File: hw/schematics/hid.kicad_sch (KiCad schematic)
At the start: 124 parts, among them M1 SK8701-01-005-SENSOR, SW1 SW_Push, SW10 SW_Push, SW11 SW_Push, SW12 SW_Push, SW13 SW_Push, SW14 SW_Push, SW15 SW_Push, SW16 SW_Push, SW17 SW_Push, SW18 SW_Push, SW19 SW_Push, SW2 SW_Push, SW20 SW_Push, SW21 SW_Push, SW3 SW_Push, SW4 SW_Push, SW5 SW_Push, SW6 SW_Push, SW7 SW_Push, SW8 SW_Push, SW9 SW_Push, U3 ADS122S14

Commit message: Add a bunch of models and footprints
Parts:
- C10, C11, C9, rC10, rC11, rC9: footprint Alidade:0603 -> Alidade:C_0603_1608Metric
- R10, R11, R12, R13, R14, R15, R16, R7, R8, R9, rR10, rR11, rR12, rR13, rR14, rR15, rR16, rR7, rR8, rR9: footprint Alidade:0603 -> Alidade:R_0603_1608Metric
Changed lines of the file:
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@@
 			)
 		)
-		(property "Footprint" "Alidade:0603"
+		(property "Footprint" "Alidade:C_0603_1608Metric"
 			(at 158.75 219.71 0)
 			(effects
@@
 			)
 		)
-		(property "Footprint" "Alidade:0603"
+		(property "Footprint" "Alidade:R_0603_1608Metric"
 			(at 46.99 118.11 0)
 			(effects
@@
 			)
 		)
-		(property "Footprint" "Alidade:0603"
+		(property "Footprint" "Alidade:R_0603_1608Metric"
 			(at 342.9 199.39 0)
 			(effects
@@
 			)
 		)
-		(property "Footprint" "Alidade:0603"
+		(property "Footprint" "Alidade:C_0603_1608Metric"
 			(at 34.29 217.17 0)
 			(effects
@@
 			)
 		)
-		(property "Footprint" "Alidade:0603"
+		(property "Footprint" "Alidade:R_0603_1608Metric"
 			(at 304.8 200.66 0)
 			(effects
@@
 			)
 		)
-		(property "Footprint" "Alidade:0603"
+		(property "Footprint" "Alidade:C_0603_1608Metric"
 			(at 167.64 219.71 0)
 			(effects
@@
 			)
 		)
-		(property "Footprint" "Alidade:0603"
+		(property "Footprint" "Alidade:R_0603_1608Metric"
 			(at 374.65 118.11 0)
 			(effects
@@
 			)
 		)
-		(property "Footprint" "Alidade:0603"
+		(property "Footprint" "Alidade:C_0603_1608Metric"
 			(at 149.86 219.71 0)
 			(effects
@@
 			)
 		)
-		(property "Footprint" "Alidade:0603"
+		(property "Footprint" "Alidade:R_0603_1608Metric"
 			(at 279.4 200.66 0)
 			(effects
@@
 			)
 		)
-		(property "Footprint" "Alidade:0603"
+		(property "Footprint" "Alidade:R_0603_1608Metric"
 			(at 342.9 189.23 0)
 			(effects
@@
 			)
 		)
-		(property "Footprint" "Alidade:0603"
+		(property "Footprint" "Alidade:R_0603_1608Metric"
 			(at 46.99 102.87 0)
 			(effects
@@
 			)
 		)
-		(property "Footprint" "Alidade:0603"
+		(property "Footprint" "Alidade:R_0603_1608Metric"
 			(at 374.65 87.63 0)
 			(effects
@@
 			)
 		)
-		(property "Footprint" "Alidade:0603"
+		(property "Footprint" "Alidade:R_0603_1608Metric"
 			(at 279.4 190.5 0)
 			(effects
@@
 			)
 		)
-		(property "Footprint" "Alidade:0603"
+		(property "Footprint" "Alidade:R_0603_1608Metric"
 			(at 304.8 190.5 0)
 			(effects
@@
 			)
 		)
-		(property "Footprint" "Alidade:0603"
+		(property "Footprint" "Alidade:R_0603_1608Metric"
 			(at 76.2 246.38 0)
 			(effects
@@
 			)
 		)
-		(property "Footprint" "Alidade:0603"
+		(property "Footprint" "Alidade:R_0603_1608Metric"
 			(at 46.99 72.39 0)
 			(effects
@@
 			)
 		)
-		(property "Footprint" "Alidade:0603"
+		(property "Footprint" "Alidade:R_0603_1608Metric"
 			(at 368.3 189.23 0)
 			(effects
@@
 			)
 		)
-		(property "Footprint" "Alidade:0603"
+		(property "Footprint" "Alidade:R_0603_1608Metric"
 			(at 200.66 248.92 0)
 			(effects
@@
 			)
 		)
-		(property "Footprint" "Alidade:0603"
+		(property "Footprint" "Alidade:R_0603_1608Metric"
 			(at 368.3 199.39 0)
 			(effects
@@
 			)
 		)
-		(property "Footprint" "Alidade:0603"
+		(property "Footprint" "Alidade:R_0603_1608Metric"
 			(at 46.99 87.63 0)
 			(effects
@@
 			)
 		)
-		(property "Footprint" "Alidade:0603"
+		(property "Footprint" "Alidade:C_0603_1608Metric"
 			(at 25.4 217.17 0)
 			(effects
@@
 			)
 		)
-		(property "Footprint" "Alidade:0603"
+		(property "Footprint" "Alidade:R_0603_1608Metric"
 			(at 76.2 254 0)
 			(effects
@@
 			)
 		)
-		(property "Footprint" "Alidade:0603"
+		(property "Footprint" "Alidade:C_0603_1608Metric"
 			(at 43.18 217.17 0)
 			(effects
@@
 			)
 		)
-		(property "Footprint" "Alidade:0603"
+		(property "Footprint" "Alidade:R_0603_1608Metric"
 			(at 374.65 72.39 0)
 			(effects
@@
 			)
 		)
-		(property "Footprint" "Alidade:0603"
+		(property "Footprint" "Alidade:R_0603_1608Metric"
 			(at 200.66 256.54 0)
 			(effects
@@
 			)
 		)
-		(property "Footprint" "Alidade:0603"
+		(property "Footprint" "Alidade:R_0603_1608Metric"
 			(at 374.65 102.87 0)
 			(effects

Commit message: Various footprint updates
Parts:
- removed U3, rU3: ADS122S14, Alidade:RTE0016C-MFG, symbol Alidade:ADS122S14
- added U3, rU3: ADS122S14IRTER, Alidade:WQFN16_3X3, symbol Alidade:ADS122S14IRTER
- SWD1, rSWD1: footprint (none) -> Alidade:228ADS2
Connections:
- net ADCCS: now also U3.9 (CS)
- net AIN0: now also U3.1 (AIN0)
- net AIN1: now also U3.2 (AIN1)
- net AVDD: now also U3.15 (AVDD)
- net DRDY: now also U3.8 (AIN7/GPIO3/DRDY/CLK)
- net DVDD: now also U3.13 (DVDD)
- net FAULT: now also U3.7 (AIN6/GPIO2/FAULT)
- net GND: now also U3.14 (GND), U3.TP
- net MISO: now also U3.10 (SDO/DRDY)
- net MOSI: now also U3.11 (SDI)
- net REFN: now also U3.6 (AIN5/REFN/GPIO1)
- net REFP: now also U3.5 (AIN4/REFP/GPIO0)
- net SCK: now also U3.12 (SCK)
- net rADCCS: now also rU3.9 (CS)
- net rAIN0: now also rU3.1 (AIN0)
- net rAIN1: now also rU3.2 (AIN1)
- net rAVDD: now also rU3.15 (AVDD)
- net rDRDY: now also rU3.8 (AIN7/GPIO3/DRDY/CLK)
- net rDVDD: now also rU3.13 (DVDD)
- net rFAULT: now also rU3.7 (AIN6/GPIO2/FAULT)
- net rGND: now also rU3.14 (GND), rU3.TP
- net rMISO: now also rU3.10 (SDO/DRDY)
- net rMOSI: now also rU3.11 (SDI)
- net rREFN: now also rU3.6 (AIN5/REFN/GPIO1)
- net rREFP: now also rU3.5 (AIN4/REFP/GPIO0)
- net rSCK: now also rU3.12 (SCK)
- net at R15.2, R16.1: now also U3.3 (AIN2)
- net at rC11.1: now also rU3.16 (REFOUT)
- net at C11.1: now also U3.16 (REFOUT)
- net at rR15.2, rR16.1: now also rU3.3 (AIN2)

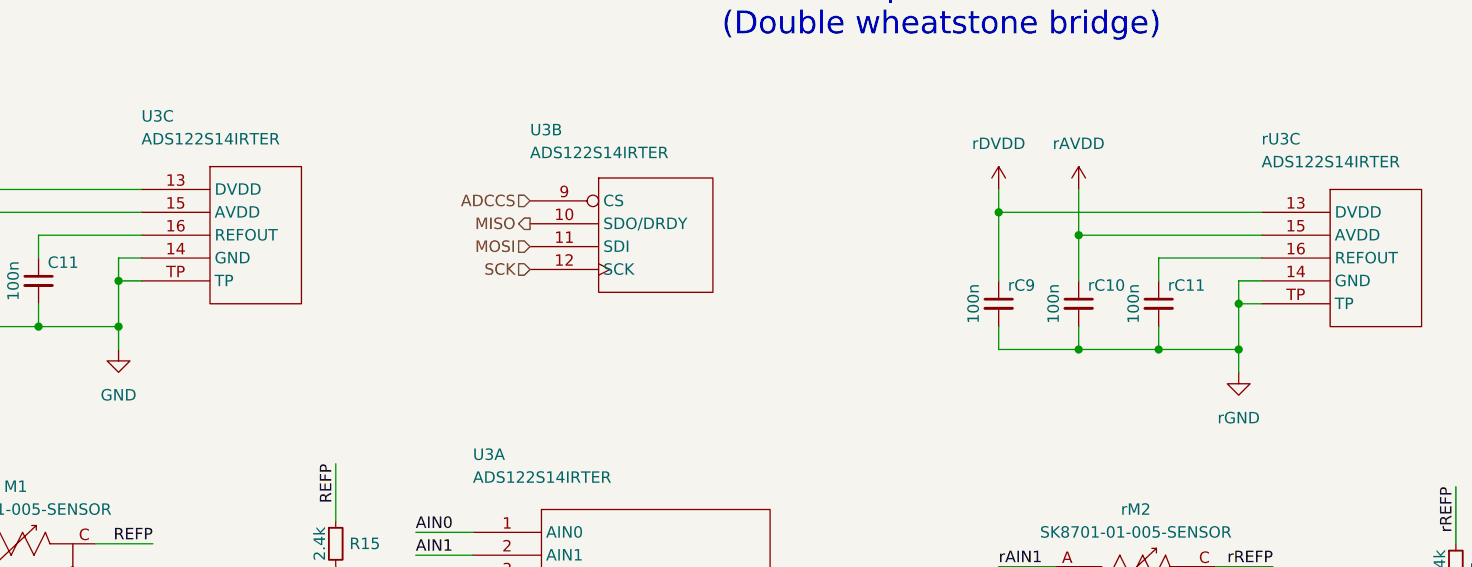
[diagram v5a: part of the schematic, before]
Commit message: Fix missing pads
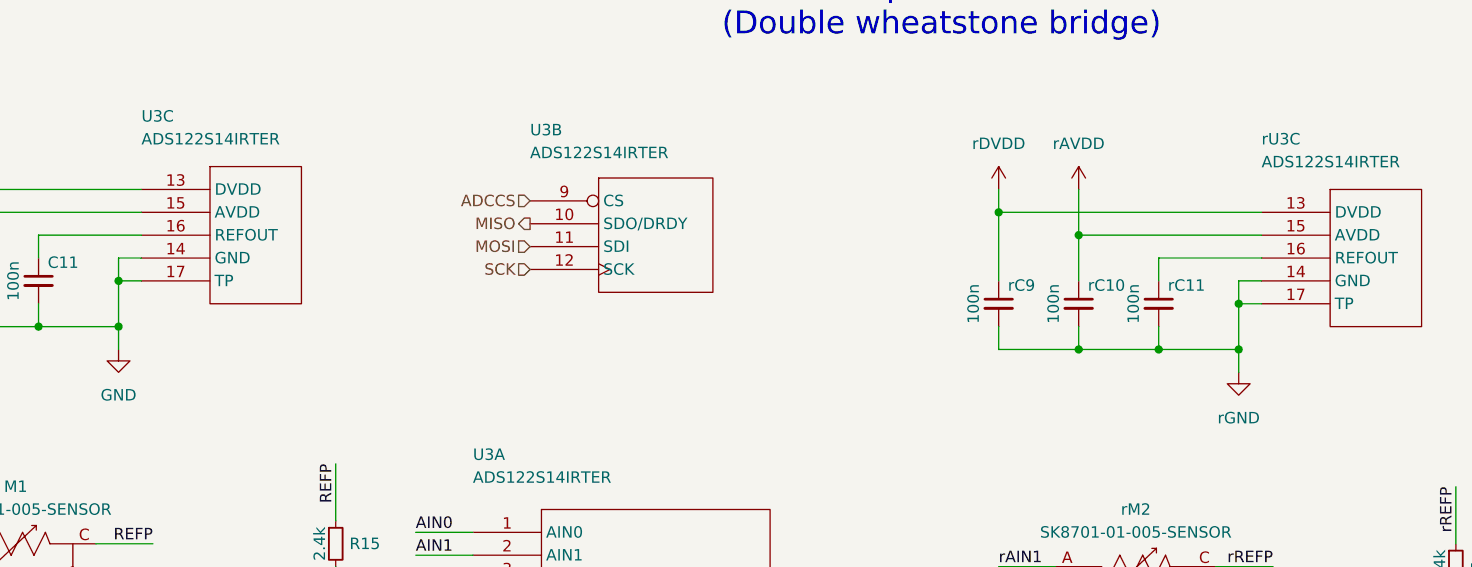
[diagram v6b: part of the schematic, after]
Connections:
- net GND: now also U3.17 (TP); no longer U3.TP
- net rGND: now also rU3.17 (TP); no longer rU3.TP
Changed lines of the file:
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@@
 		(pin "13"
 		)
-		(pin "TP"
+		(pin "17"
 		)
 		(pin "11"
@@
 		(pin "2"
 		)
-		(pin "MH2"
-		)
 		(pin "4"
 		)
@@
 		(pin "L1"
 		)
-		(pin "MH1"
-		)
 		(instances
 			(project ""
@@
 		(pin "13"
 		)
-		(pin "TP"
+		(pin "17"
 		)
 		(pin "11"
@@
 		(pin "13"
 		)
-		(pin "TP"
+		(pin "17"
 		)
 		(pin "11"
@@
 		(pin "13"
 		)
-		(pin "TP"
+		(pin "17"
 		)
 		(pin "11"
@@
 		(pin "3"
 		)
-		(pin "MH1"
-		)
-		(pin "MH2"
-		)
 		(pin "L1"
 		)
@@
 		(pin "13"
 		)
-		(pin "TP"
+		(pin "17"
 		)
 		(pin "11"
@@
 		(pin "2"
 		)
-		(pin "MH2"
-		)
 		(pin "4"
 		)
@@
 		(pin "3"
 		)
-		(pin "MH1"
-		)
 		(pin "L2"
 		)
@@
 			)
 		)
-		(pin "MH1"
-		)
 		(pin "2"
 		)
@@
 		(pin "3"
 		)
-		(pin "MH2"
-		)
 		(pin "1"
 		)
@@
 		(pin "13"
 		)
-		(pin "TP"
+		(pin "17"
 		)
 		(pin "11"

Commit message: LCSC part numbers
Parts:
- C10, C11, C9, rC10, rC11, rC9: LCSC Part # (none) -> C14663
- R10, R11, R12, R7, R8, R9, rR10, rR11, rR12, rR7, rR8, rR9: LCSC Part # (none) -> C25804
- R13, R14, rR13, rR14: LCSC Part # (none) -> C21189
- R15, R16, rR15, rR16: LCSC Part # (none) -> C22940
- SWD1, rSWD1: LCSC Part # (none) -> C4364466

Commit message: Soldered switches
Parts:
- EXSW1, EXSW2, SW10, SW11, SW12, SW13, SW14, SW15, SW16, SW17, SW18, SW19, SW2, SW20, SW21, SW3, SW4, SW5, SW6, SW7, SW8, SW9, rEXSW1, rEXSW2, rSW10, rSW11, rSW12, rSW13, rSW14, rSW15, rSW16, rSW17, rSW18, rSW19, rSW2, rSW20, rSW21, rSW3, rSW4, rSW5, rSW6, rSW7, rSW8, rSW9: footprint Alidade:keyswitch_cherrymx_hotswap_1u -> Alidade:CherryMX_ChocV2_1u
- SW1, rSW1: footprint Alidade:keyswitch_cherrymx_hotswap_1.5u -> Alidade:CherryMX_ChocV2_1.5u
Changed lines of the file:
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@@
 			)
 		)
-		(property "Footprint" "Alidade:keyswitch_cherrymx_hotswap_1u"
+		(property "Footprint" "Alidade:CherryMX_ChocV2_1u"
 			(at 287.02 81.28 0)
 			(effects
@@
 			)
 		)
-		(property "Footprint" "Alidade:keyswitch_cherrymx_hotswap_1u"
+		(property "Footprint" "Alidade:CherryMX_ChocV2_1u"
 			(at 267.97 66.04 0)
 			(effects
@@
 			)
 		)
-		(property "Footprint" "Alidade:keyswitch_cherrymx_hotswap_1u"
+		(property "Footprint" "Alidade:CherryMX_ChocV2_1u"
 			(at 172.72 92.71 0)
 			(effects
@@
 			)
 		)
-		(property "Footprint" "Alidade:keyswitch_cherrymx_hotswap_1u"
+		(property "Footprint" "Alidade:CherryMX_ChocV2_1u"
 			(at 115.57 96.52 0)
 			(effects
@@
 			)
 		)
-		(property "Footprint" "Alidade:keyswitch_cherrymx_hotswap_1u"
+		(property "Footprint" "Alidade:CherryMX_ChocV2_1u"
 			(at 115.57 111.76 0)
 			(effects
@@
 			)
 		)
-		(property "Footprint" "Alidade:keyswitch_cherrymx_hotswap_1u"
+		(property "Footprint" "Alidade:CherryMX_ChocV2_1u"
 			(at 287.02 66.04 0)
 			(effects
@@
 			)
 		)
-		(property "Footprint" "Alidade:keyswitch_cherrymx_hotswap_1u"
+		(property "Footprint" "Alidade:CherryMX_ChocV2_1u"
 			(at 344.17 96.52 0)
 			(effects
@@
 			)
 		)
-		(property "Footprint" "Alidade:keyswitch_cherrymx_hotswap_1.5u"
+		(property "Footprint" "Alidade:CherryMX_ChocV2_1.5u"
 			(at 153.67 111.76 0)
 			(effects
@@
 			)
 		)
-		(property "Footprint" "Alidade:keyswitch_cherrymx_hotswap_1u"
+		(property "Footprint" "Alidade:CherryMX_ChocV2_1u"
 			(at 325.12 96.52 0)
 			(effects
@@
 			)
 		)
-		(property "Footprint" "Alidade:keyswitch_cherrymx_hotswap_1u"
+		(property "Footprint" "Alidade:CherryMX_ChocV2_1u"
 			(at 115.57 66.04 0)
 			(effects
@@
 			)
 		)
-		(property "Footprint" "Alidade:keyswitch_cherrymx_hotswap_1u"
+		(property "Footprint" "Alidade:CherryMX_ChocV2_1u"
 			(at 77.47 96.52 0)
 			(effects
@@
 			)
 		)
-		(property "Footprint" "Alidade:keyswitch_cherrymx_hotswap_1.5u"
+		(property "Footprint" "Alidade:CherryMX_ChocV2_1.5u"
 			(at 267.97 111.76 0)
 			(effects
@@
 			)
 		)
-		(property "Footprint" "Alidade:keyswitch_cherrymx_hotswap_1u"
+		(property "Footprint" "Alidade:CherryMX_ChocV2_1u"
 			(at 153.67 81.28 0)
 			(effects
@@
 			)
 		)
-		(property "Footprint" "Alidade:keyswitch_cherrymx_hotswap_1u"
+		(property "Footprint" "Alidade:CherryMX_ChocV2_1u"
 			(at 134.62 81.28 0)
 			(effects
@@
 			)
 		)
-		(property "Footprint" "Alidade:keyswitch_cherrymx_hotswap_1u"
+		(property "Footprint" "Alidade:CherryMX_ChocV2_1u"
 			(at 134.62 96.52 0)
 			(effects
@@
 			)
 		)
-		(property "Footprint" "Alidade:keyswitch_cherrymx_hotswap_1u"
+		(property "Footprint" "Alidade:CherryMX_ChocV2_1u"
 			(at 344.17 81.28 0)
 			(effects
@@
 			)
 		)
-		(property "Footprint" "Alidade:keyswitch_cherrymx_hotswap_1u"
+		(property "Footprint" "Alidade:CherryMX_ChocV2_1u"
 			(at 361.95 96.52 0)
 			(effects
@@
 			)
 		)
-		(property "Footprint" "Alidade:keyswitch_cherrymx_hotswap_1u"
+		(property "Footprint" "Alidade:CherryMX_ChocV2_1u"
 			(at 306.07 111.76 0)
 			(effects
@@
 			)
 		)
-		(property "Footprint" "Alidade:keyswitch_cherrymx_hotswap_1u"
+		(property "Footprint" "Alidade:CherryMX_ChocV2_1u"
 			(at 153.67 66.04 0)
 			(effects
@@
 			)
 		)
-		(property "Footprint" "Alidade:keyswitch_cherrymx_hotswap_1u"
+		(property "Footprint" "Alidade:CherryMX_ChocV2_1u"
 			(at 361.95 66.04 0)
 			(effects
@@
 			)
 		)
-		(property "Footprint" "Alidade:keyswitch_cherrymx_hotswap_1u"
+		(property "Footprint" "Alidade:CherryMX_ChocV2_1u"
 			(at 267.97 96.52 0)
 			(effects
@@
 			)
 		)
-		(property "Footprint" "Alidade:keyswitch_cherrymx_hotswap_1u"
+		(property "Footprint" "Alidade:CherryMX_ChocV2_1u"
 			(at 325.12 66.04 0)
 			(effects
@@
 			)
 		)
-		(property "Footprint" "Alidade:keyswitch_cherrymx_hotswap_1u"
+		(property "Footprint" "Alidade:CherryMX_ChocV2_1u"
 			(at 115.57 81.28 0)
 			(effects
@@
 			)
 		)
-		(property "Footprint" "Alidade:keyswitch_cherrymx_hotswap_1u"
+		(property "Footprint" "Alidade:CherryMX_ChocV2_1u"
 			(at 96.52 66.04 0)
 			(effects
@@
 			)
 		)
-		(property "Footprint" "Alidade:keyswitch_cherrymx_hotswap_1u"
+		(property "Footprint" "Alidade:CherryMX_ChocV2_1u"
 			(at 172.72 77.47 0)
 			(effects
@@
 			)
 		)
-		(property "Footprint" "Alidade:keyswitch_cherrymx_hotswap_1u"
+		(property "Footprint" "Alidade:CherryMX_ChocV2_1u"
 			(at 248.92 92.71 0)
 			(effects
@@
 			)
 		)
-		(property "Footprint" "Alidade:keyswitch_cherrymx_hotswap_1u"
+		(property "Footprint" "Alidade:CherryMX_ChocV2_1u"
 			(at 287.02 96.52 0)
 			(effects
@@
 			)
 		)
-		(property "Footprint" "Alidade:keyswitch_cherrymx_hotswap_1u"
+		(property "Footprint" "Alidade:CherryMX_ChocV2_1u"
 			(at 325.12 81.28 0)
 			(effects
@@
 			)
 		)
-		(property "Footprint" "Alidade:keyswitch_cherrymx_hotswap_1u"
+		(property "Footprint" "Alidade:CherryMX_ChocV2_1u"
 			(at 134.62 66.04 0)
 			(effects
@@
 			)
 		)
-		(property "Footprint" "Alidade:keyswitch_cherrymx_hotswap_1u"
+		(property "Footprint" "Alidade:CherryMX_ChocV2_1u"
 			(at 96.52 81.28 0)
 			(effects
@@
 			)
 		)
-		(property "Footprint" "Alidade:keyswitch_cherrymx_hotswap_1u"
+		(property "Footprint" "Alidade:CherryMX_ChocV2_1u"
 			(at 77.47 66.04 0)
 			(effects
@@
 			)
 		)
-		(property "Footprint" "Alidade:keyswitch_cherrymx_hotswap_1u"
+		(property "Footprint" "Alidade:CherryMX_ChocV2_1u"
 			(at 77.47 81.28 0)
 			(effects
@@
 			)
 		)
-		(property "Footprint" "Alidade:keyswitch_cherrymx_hotswap_1u"
+		(property "Footprint" "Alidade:CherryMX_ChocV2_1u"
 			(at 267.97 81.28 0)
 			(effects
@@
 			)
 		)
-		(property "Footprint" "Alidade:keyswitch_cherrymx_hotswap_1u"
+		(property "Footprint" "Alidade:CherryMX_ChocV2_1u"
 			(at 59.69 96.52 0)
 			(effects
@@
 			)
 		)
-		(property "Footprint" "Alidade:keyswitch_cherrymx_hotswap_1u"
+		(property "Footprint" "Alidade:CherryMX_ChocV2_1u"
 			(at 361.95 81.28 0)
 			(effects
@@
 			)
 		)
-		(property "Footprint" "Alidade:keyswitch_cherrymx_hotswap_1u"
+		(property "Footprint" "Alidade:CherryMX_ChocV2_1u"
 			(at 59.69 81.28 0)
 			(effects
@@
 			)
 		)
-		(property "Footprint" "Alidade:keyswitch_cherrymx_hotswap_1u"
+		(property "Footprint" "Alidade:CherryMX_ChocV2_1u"
 			(at 306.07 81.28 0)
 			(effects
@@
 			)
 		)
-		(property "Footprint" "Alidade:keyswitch_cherrymx_hotswap_1u"
+		(property "Footprint" "Alidade:CherryMX_ChocV2_1u"
 			(at 134.62 111.76 0)
 			(effects
@@
 			)
 		)
-		(property "Footprint" "Alidade:keyswitch_cherrymx_hotswap_1u"
+		(property "Footprint" "Alidade:CherryMX_ChocV2_1u"
 			(at 344.17 66.04 0)
 			(effects
@@
 			)
 		)
-		(property "Footprint" "Alidade:keyswitch_cherrymx_hotswap_1u"
+		(property "Footprint" "Alidade:CherryMX_ChocV2_1u"
 			(at 287.02 111.76 0)
 			(effects
@@
 			)
 		)
-		(property "Footprint" "Alidade:keyswitch_cherrymx_hotswap_1u"
+		(property "Footprint" "Alidade:CherryMX_ChocV2_1u"
 			(at 153.67 96.52 0)
 			(effects
@@
 			)
 		)
-		(property "Footprint" "Alidade:keyswitch_cherrymx_hotswap_1u"
+		(property "Footprint" "Alidade:CherryMX_ChocV2_1u"
 			(at 306.07 96.52 0)
 			(effects
@@
 			)
 		)
-		(property "Footprint" "Alidade:keyswitch_cherrymx_hotswap_1u"
+		(property "Footprint" "Alidade:CherryMX_ChocV2_1u"
 			(at 306.07 66.04 0)
 			(effects
@@
 			)
 		)
-		(property "Footprint" "Alidade:keyswitch_cherrymx_hotswap_1u"
+		(property "Footprint" "Alidade:CherryMX_ChocV2_1u"
 			(at 96.52 96.52 0)
 			(effects
@@
 			)
 		)
-		(property "Footprint" "Alidade:keyswitch_cherrymx_hotswap_1u"
+		(property "Footprint" "Alidade:CherryMX_ChocV2_1u"
 			(at 248.92 77.47 0)
 			(effects
@@
 			)
 		)
-		(property "Footprint" "Alidade:keyswitch_cherrymx_hotswap_1u"
+		(property "Footprint" "Alidade:CherryMX_ChocV2_1u"
 			(at 59.69 66.04 0)
 			(effects
